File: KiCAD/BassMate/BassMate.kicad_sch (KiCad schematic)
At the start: 38 parts, among them J2 Conn_01x04, J3 Conn_01x04, J4 Conn_01x05, J5 Conn_01x05, J6 Barrel_Jack, J7 Conn_01x05, J8 Conn_01x04, U1 LM78M33, U2 BlackPill411, U3 LM7805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

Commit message: Update schematic for AD5204. Better 3D case model.
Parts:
- removed D?: D, symbol Device:D
- removed J7: Conn_01x05, Connector_PinHeader_2.54mm:PinHeader_1x05_P2.54mm_Vertical, symbol Connector_Generic:Conn_01x05
- added C? (x2): 100u, Capacitor_THT:CP_Radial_D10.0mm_P3.50mm, symbol Device:C_Polarized
- added C? (x2): C, Capacitor_THT:C_Disc_D5.0mm_W2.5mm_P2.50mm, symbol Device:C
- added D?: BR, symbol Device:D_Bridge_+-AA
- added J?: Conn_01x05, Connector_PinHeader_2.54mm:PinHeader_1x05_P2.54mm_Vertical, symbol Connector_Generic:Conn_01x05
- added J?: Conn_01x02, symbol Connector_Generic:Conn_01x02
- added U?: LM7805, Package_TO_SOT_THT:TO-220-3_Vertical, symbol Regulator_Linear:LM7805_TO220
- C7: value C_Polarized -> 4700u
- J6: value Barrel_Jack -> 9V
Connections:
- net +5V: now also C?.1, C?.1, U?.3 (VO); no longer C6.1, C7.1, U3.3 (VO), U5.1 (+5V)
- net +9V: now also C?.1, C?.1, D?.1 (+), U?.1 (VI)
- net GND: now also C?.2, C?.2, C?.2, C?.2, D?.2 (-), J?.2 (Pin_2), J?.4 (Pin_4), U?.2 (GND); no longer J6.2
- net at R3.2: now also U5.5 (R_IN), J?.1 (Pin_1); no longer U5.3 (L_IN)
- net at R2.2: now also U5.3 (L_IN), J?.2 (Pin_2); no longer U5.5 (R_IN)
- net at U4.16 (ROUT): now also J?.5 (Pin_5)
- net at U4.15 (LOUT): now also J?.3 (Pin_3)
- net at J6.1: now also D?.3
- net DPSCK: now reaches U2.10 (A4)
- net DPCS: now reaches U2.17 (B10)
- net +3V3: now reaches U2.41 (3V3)
- net DPSDI: now reaches U2.9 (A3)
- net +3.3VA: now reaches U4.21 (3V3)
- net +3.3VA: now also J?.1 (Pin_1)
- new net: C6.1, C7.1, U3.3 (VO), U5.1 (+5V)
- new net: D?.4, J6.2
- no-connect marks 35 -> 30
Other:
- added sheet Volume Board (VolumeBoard.kicad_sch)
- moved on the sheet: J8, R2, R3, U5

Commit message: Started docs
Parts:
- removed #J7: AudioJack3_Dual_Switch, symbol Connector:AudioJack3_Dual_Switch
- added PS?: Generic buck converter module, Converter_DCDC:Converter_DCDC_XP_POWER-ITXxxxxSA_THT, symbol Converter_DCDC:ITX4803SA
- C1, C4, C5, C6, C? (x2): value C -> 100n
- C3: value C_Polarized -> 100u
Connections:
- net at D?.3: now also PS?.6 (+Vout); no longer J6.1
- net at D?.4: now also PS?.7 (-Vout); no longer J6.2
- new net: J6.2, PS?.1 (-Vin)
- new net: J6.1, PS?.2 (+Vin)
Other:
- note added: "Amplifier"
- note added: "Max current = 20mA per pixel per color = 20 * 3 * 8 * 4 = 1.92A!! => Limit the maximum brightness and never use white"
- note added: "Power Supply"
- note added: "Speaker(s) Offboard"
- note added: "This whole section makes no sense. Powered from 9V directly, the LM805 regulators got a bit hotter than I'd like so I stuck the buck converter in front to lower their input voltage and get the power consumption down. I should probably test to see if everything would work OK with just two buck converters for 5V and 3V3, but I can't be bothered at this point :-)"
- note removed: "Max current = 20mA per pixel per color = 20 * 3 * 8 * 4 = 1.92A!!"
- moved on the sheet: C?, D?, J6

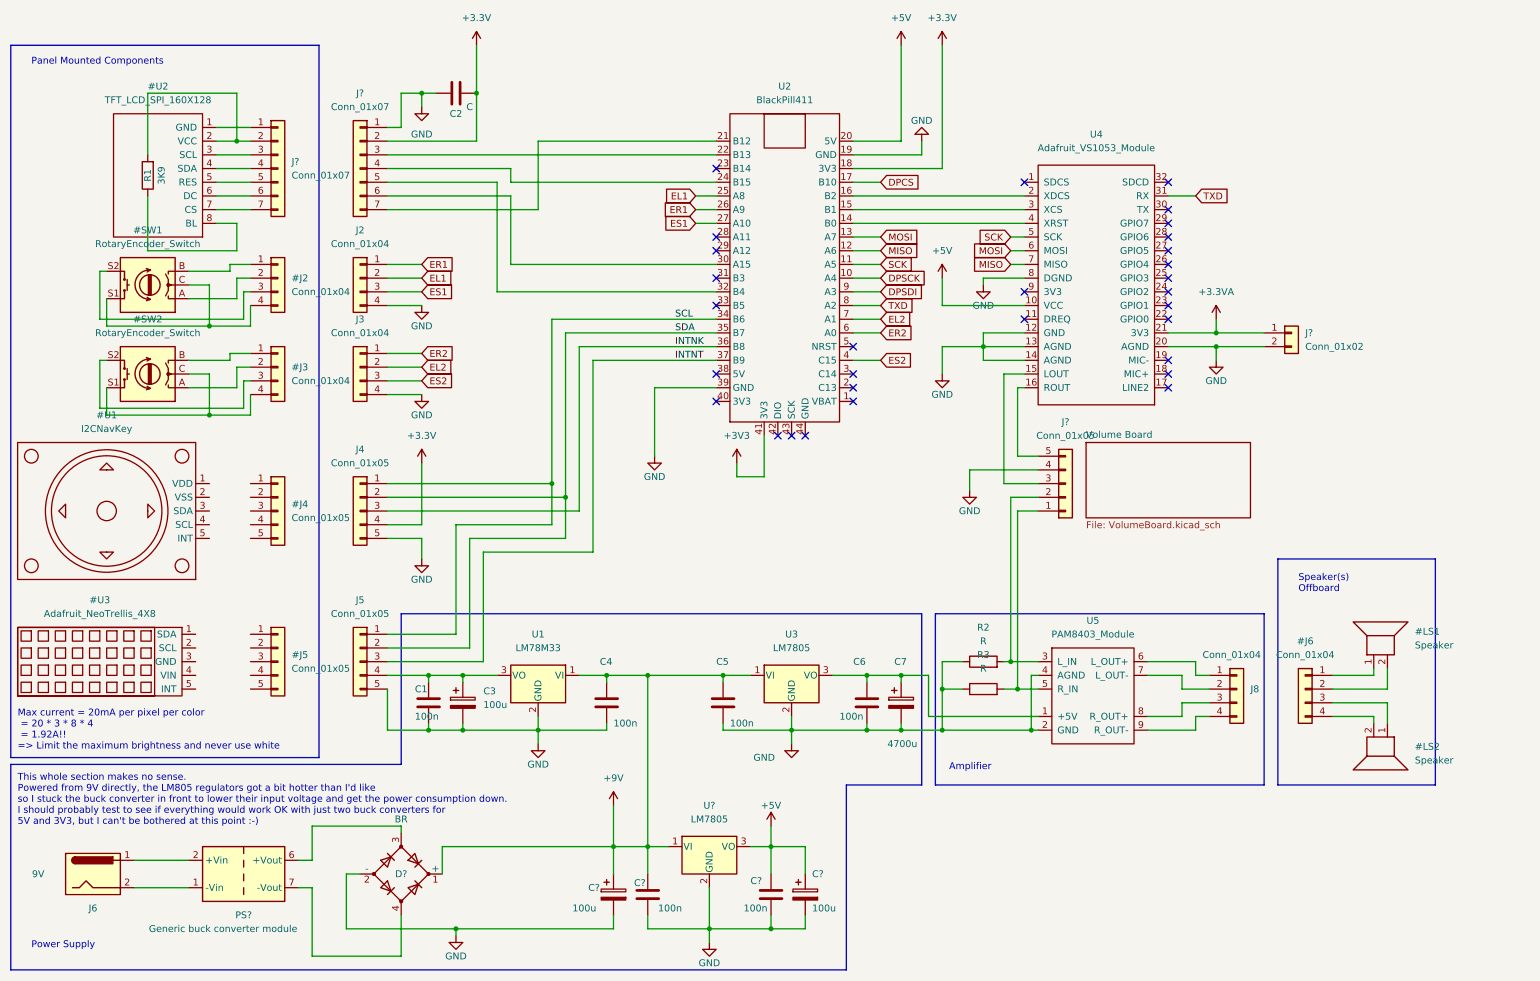
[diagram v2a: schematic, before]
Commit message: Converted most libs to git sbmodules
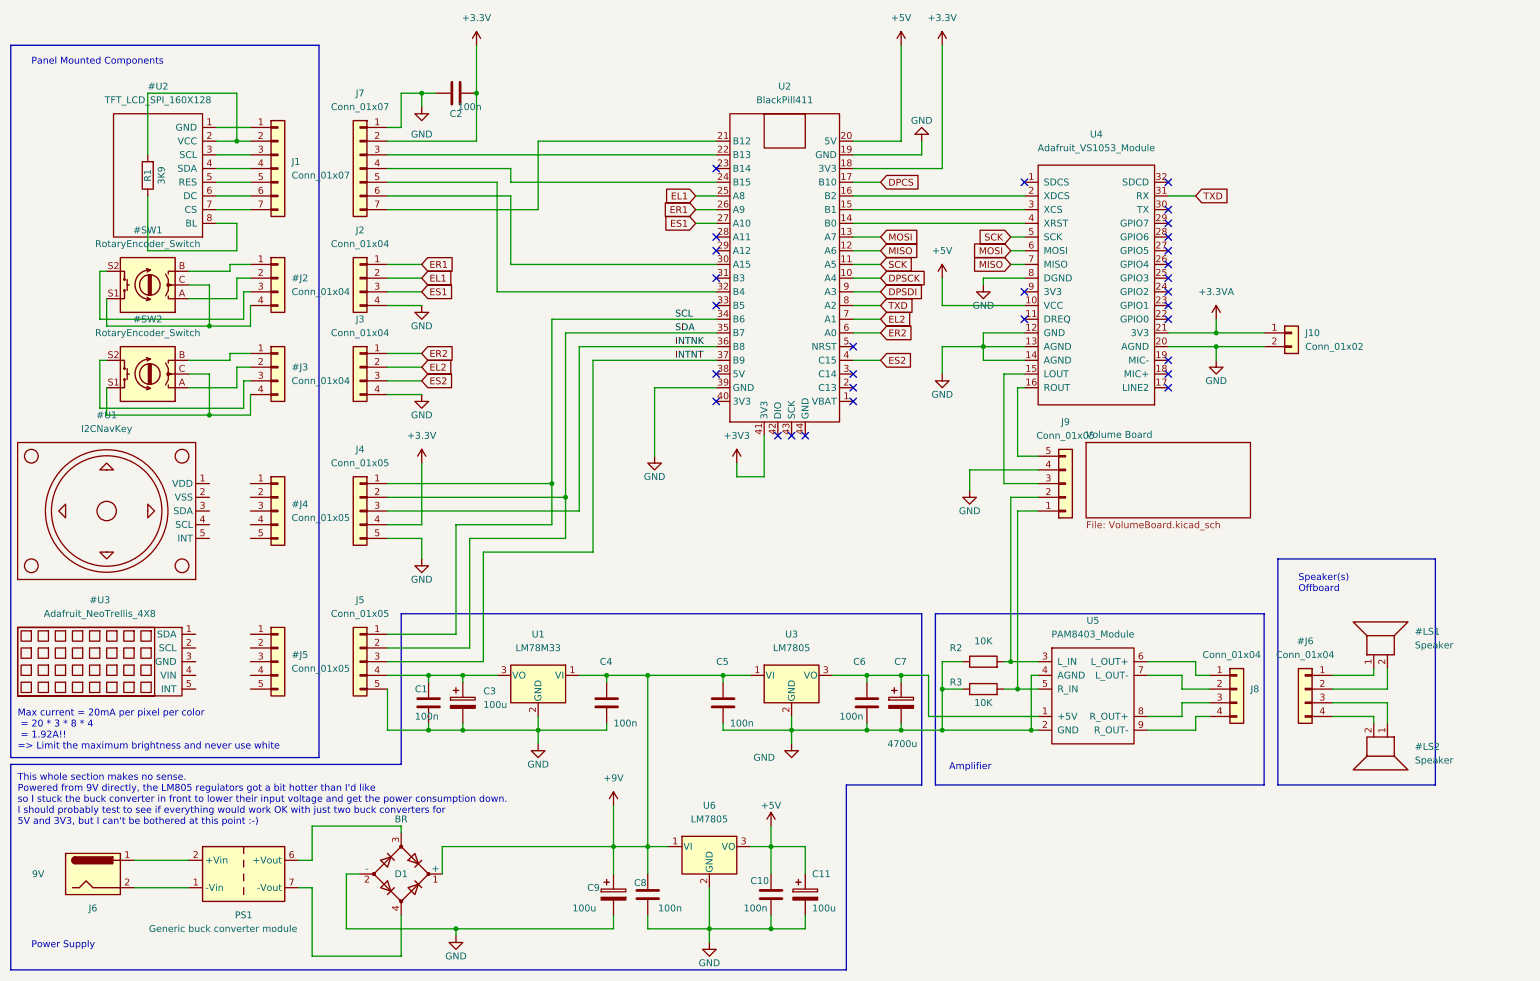
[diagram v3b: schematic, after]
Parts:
- C2: value C -> 100n
- R2, R3: value R -> 10K
- gave numbers to parts that had none: 11
